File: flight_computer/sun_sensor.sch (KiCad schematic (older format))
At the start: 2 parts

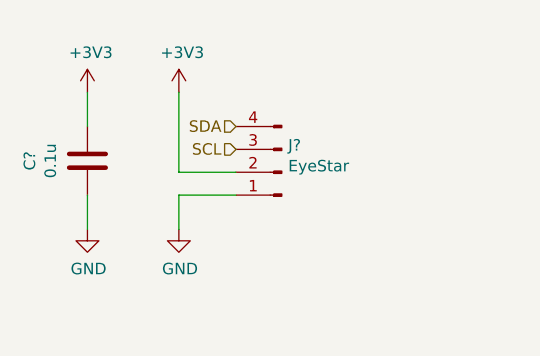
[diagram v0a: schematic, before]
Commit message: Annotating schematic with references and footprints
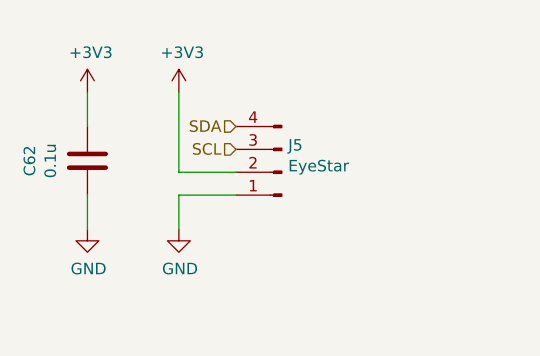
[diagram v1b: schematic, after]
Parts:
- gave numbers to parts that had none: 2
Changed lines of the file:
@@
 P 6300 4100
 AR Path="/63D2A1FC/637A6C60" Ref="J?"  Part="1"
-AR Path="/63D2A1C8/637A6C60" Ref="J?"  Part="1"
-F 0 "J?" H 6272 3982 50  0000 R CNN
+AR Path="/63D2A1C8/637A6C60" Ref="J5"  Part="1"
+F 0 "J5" H 6272 3982 50  0000 R CNN
 F 1 "EyeStar" H 6272 4073 50  0000 R CNN
 F 2 "" H 6300 4100 50  0001 C CNN
@@
 P 5850 4350
 AR Path="/63D2A1FC/637A6C66" Ref="#PWR?"  Part="1"
-AR Path="/63D2A1C8/637A6C66" Ref="#PWR?"  Part="1"
-F 0 "#PWR?" H 5850 4100 50  0001 C CNN
+AR Path="/63D2A1C8/637A6C66" Ref="#PWR0285"  Part="1"
+F 0 "#PWR0285" H 5850 4100 50  0001 C CNN
 F 1 "GND" H 5855 4177 50  0000 C CNN
 F 2 "" H 5850 4350 50  0001 C CNN
@@
 AR Path="/63D1F518/637AA27A" Ref="C?"  Part="1"
 AR Path="/63D21EEE/637AA27A" Ref="C?"  Part="1"
-AR Path="/63D2A1C8/637AA27A" Ref="C?"  Part="1"
-F 0 "C?" V 5702 4050 50  0000 C CNN
+AR Path="/63D2A1C8/637AA27A" Ref="C62"  Part="1"
+F 0 "C62" V 5702 4050 50  0000 C CNN
 F 1 "0.1u" V 5611 4050 50  0000 C CNN
 F 2 "Capacitor_SMD:C_0603_1608Metric" H 5488 3900 50  0001 C CNN
@@
 AR Path="/63D1F518/637AA281" Ref="#PWR?"  Part="1"
 AR Path="/63D21EEE/637AA281" Ref="#PWR?"  Part="1"
-F 0 "#PWR?" H 5450 4100 50  0001 C CNN
+AR Path="/63D2A1C8/637AA281" Ref="#PWR0286"  Part="1"
+F 0 "#PWR0286" H 5450 4100 50  0001 C CNN
 F 1 "GND" H 5455 4177 50  0000 C CNN
 F 2 "" H 5450 4350 50  0001 C CNN
@@
 $EndComp
 $Comp
-L power:+3V3 #PWR?
+L power:+3V3 #PWR0287
 U 1 1 637A6E58
 P 5850 3750
-F 0 "#PWR?" H 5850 3600 50  0001 C CNN
+F 0 "#PWR0287" H 5850 3600 50  0001 C CNN
 F 1 "+3V3" H 5865 3923 50  0000 C CNN
 F 2 "" H 5850 3750 50  0001 C CNN
@@
 $EndComp
 $Comp
-L power:+3V3 #PWR?
+L power:+3V3 #PWR0288
 U 1 1 637AA35F
 P 5450 3750
-F 0 "#PWR?" H 5450 3600 50  0001 C CNN
+F 0 "#PWR0288" H 5450 3600 50  0001 C CNN
 F 1 "+3V3" H 5465 3923 50  0000 C CNN
 F 2 "" H 5450 3750 50  0001 C CNN

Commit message: Continuing layout
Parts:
- removed J5: EyeStar, symbol Connector:Conn_01x04_Male
- added J5: 0781710004, 0781710004:MOLEX_0781710004, symbol 0781710004:0781710004
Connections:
- net +3V3: now also J5.2
- net GND: now also J5.1, J5.S1 (SHIELD), J5.S2 (SHIELD)
- net SCL: now also J5.3
- net SDA: now also J5.4
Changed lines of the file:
@@
 $Descr A4 11693 8268
 encoding utf-8
-Sheet 8 9
+Sheet 6 6
 Title ""
 Date ""
@@
 $EndDescr
 $Comp
-L Connector:Conn_01x04_Male J?
-U 1 1 637A6C60
-P 6300 4100
-AR Path="/63D2A1FC/637A6C60" Ref="J?"  Part="1"
-AR Path="/63D2A1C8/637A6C60" Ref="J5"  Part="1"
-F 0 "J5" H 6272 3982 50  0000 R CNN
-F 1 "EyeStar" H 6272 4073 50  0000 R CNN
-F 2 "" H 6300 4100 50  0001 C CNN
-F 3 "~" H 6300 4100 50  0001 C CNN
-	1    6300 4100
-	-1   0    0    1
-$EndComp
-$Comp
 L power:GND #PWR?
 U 1 1 637A6C66
-P 5850 4350
+P 5850 4600
 AR Path="/63D2A1FC/637A6C66" Ref="#PWR?"  Part="1"
 AR Path="/63D2A1C8/637A6C66" Ref="#PWR0285"  Part="1"
-F 0 "#PWR0285" H 5850 4100 50  0001 C CNN
-F 1 "GND" H 5855 4177 50  0000 C CNN
-F 2 "" H 5850 4350 50  0001 C CNN
-F 3 "" H 5850 4350 50  0001 C CNN
-	1    5850 4350
+F 0 "#PWR0285" H 5850 4350 50  0001 C CNN
+F 1 "GND" H 5855 4427 50  0000 C CNN
+F 2 "" H 5850 4600 50  0001 C CNN
+F 3 "" H 5850 4600 50  0001 C CNN
+	1    5850 4600
 	1    0    0    -1
 $EndComp
-Text HLabel 6100 4000 0    50   Input ~ 0
+Text HLabel 6100 4100 0    50   Input ~ 0
 SCL
-Text HLabel 6100 3900 0    50   Input ~ 0
+Text HLabel 6100 4200 0    50   Input ~ 0
 SDA
 Wire Wire Line
-	6100 4100 5850 4100
+	5800 4000 5800 3650
 Wire Wire Line
-	5850 4100 5850 3750
-Wire Wire Line
-	6100 4200 5850 4200
-Wire Wire Line
-	5850 4200 5850 4350
+	6100 3900 5850 3900
 $Comp
 L Device:C C?
@@
 L power:+3V3 #PWR0287
 U 1 1 637A6E58
-P 5850 3750
-F 0 "#PWR0287" H 5850 3600 50  0001 C CNN
-F 1 "+3V3" H 5865 3923 50  0000 C CNN
-F 2 "" H 5850 3750 50  0001 C CNN
-F 3 "" H 5850 3750 50  0001 C CNN
-	1    5850 3750
+P 5800 3650
+F 0 "#PWR0287" H 5800 3500 50  0001 C CNN
+F 1 "+3V3" H 5815 3823 50  0000 C CNN
+F 2 "" H 5800 3650 50  0001 C CNN
+F 3 "" H 5800 3650 50  0001 C CNN
+	1    5800 3650
 	1    0    0    -1
 $EndComp
@@
 Wire Wire Line
 	5450 4200 5450 4350
+$Comp
+L 0781710004:0781710004 J5
+U 1 1 63853CF7
+P 6300 4100
+F 0 "J5" H 6830 4096 50  0000 L CNN
+F 1 "0781710004" H 6830 4005 50  0000 L CNN
+F 2 "0781710004:MOLEX_0781710004" H 6300 4100 50  0001 L BNN
+F 3 "" H 6300 4100 50  0001 L BNN
+F 4 "MOLEX" H 6300 4100 50  0001 L BNN "MANUFACTURER"
+F 5 "1.52mm" H 6300 4100 50  0001 L BNN "MAXIMUM_PACKAGE_HEIGHT"
+F 6 "Manufacturer Recommendations" H 6300 4100 50  0001 L BNN "STANDARD"
+F 7 "G" H 6300 4100 50  0001 L BNN "PARTREV"
+	1    6300 4100
+	1    0    0    -1
+$EndComp
+Wire Wire Line
+	6100 4400 5850 4400
+Wire Wire Line
+	5850 3900 5850 4400
+Wire Wire Line
+	5850 4400 5850 4600
+Connection ~ 5850 4400
+Wire Wire Line
+	5800 4000 6100 4000
 $EndSCHEMATC
